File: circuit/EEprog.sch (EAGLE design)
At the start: 27 parts, among them IC1 ATMEGA168-20P, IC2 7400N, IC3 74HCT574N, IC4 74HCT574N, X1 PN61729-S

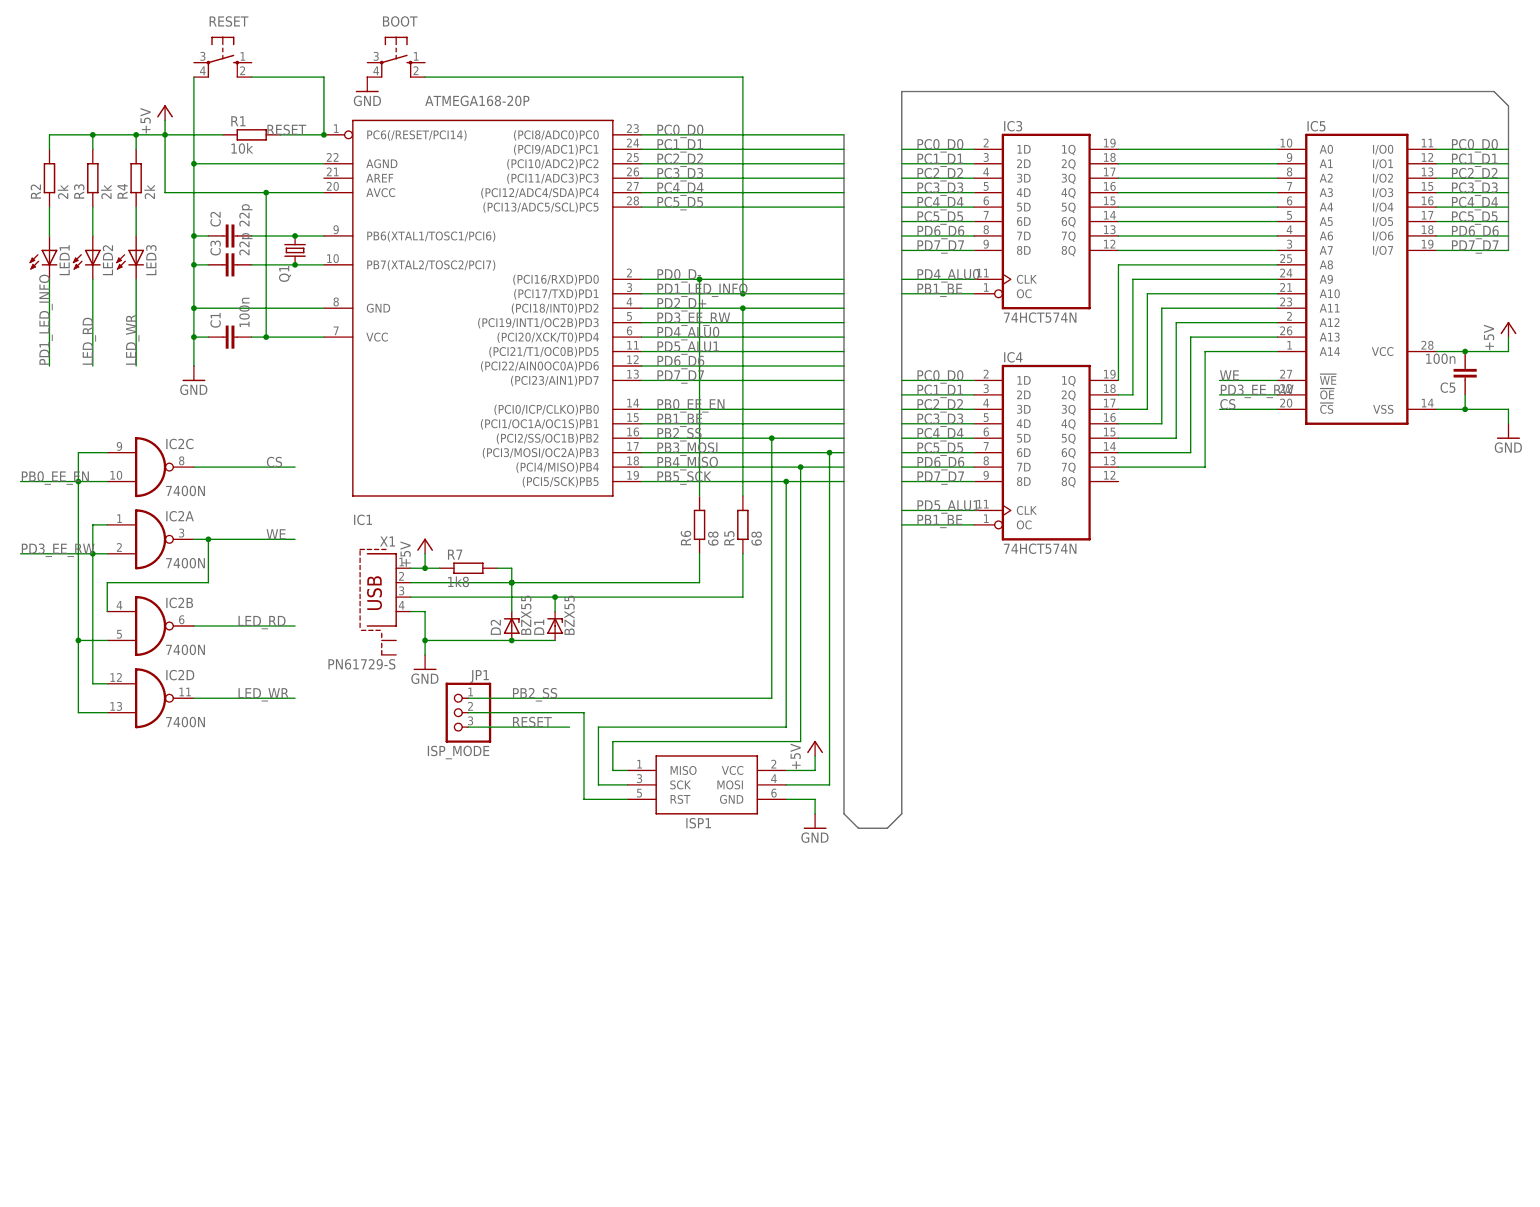
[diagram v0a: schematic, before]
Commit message: updated circuit
durring coldstart of MCU eeprom cell 0x0000 was erased with 0xff value.
pull-down registors on ce & rw control pins fixed issue
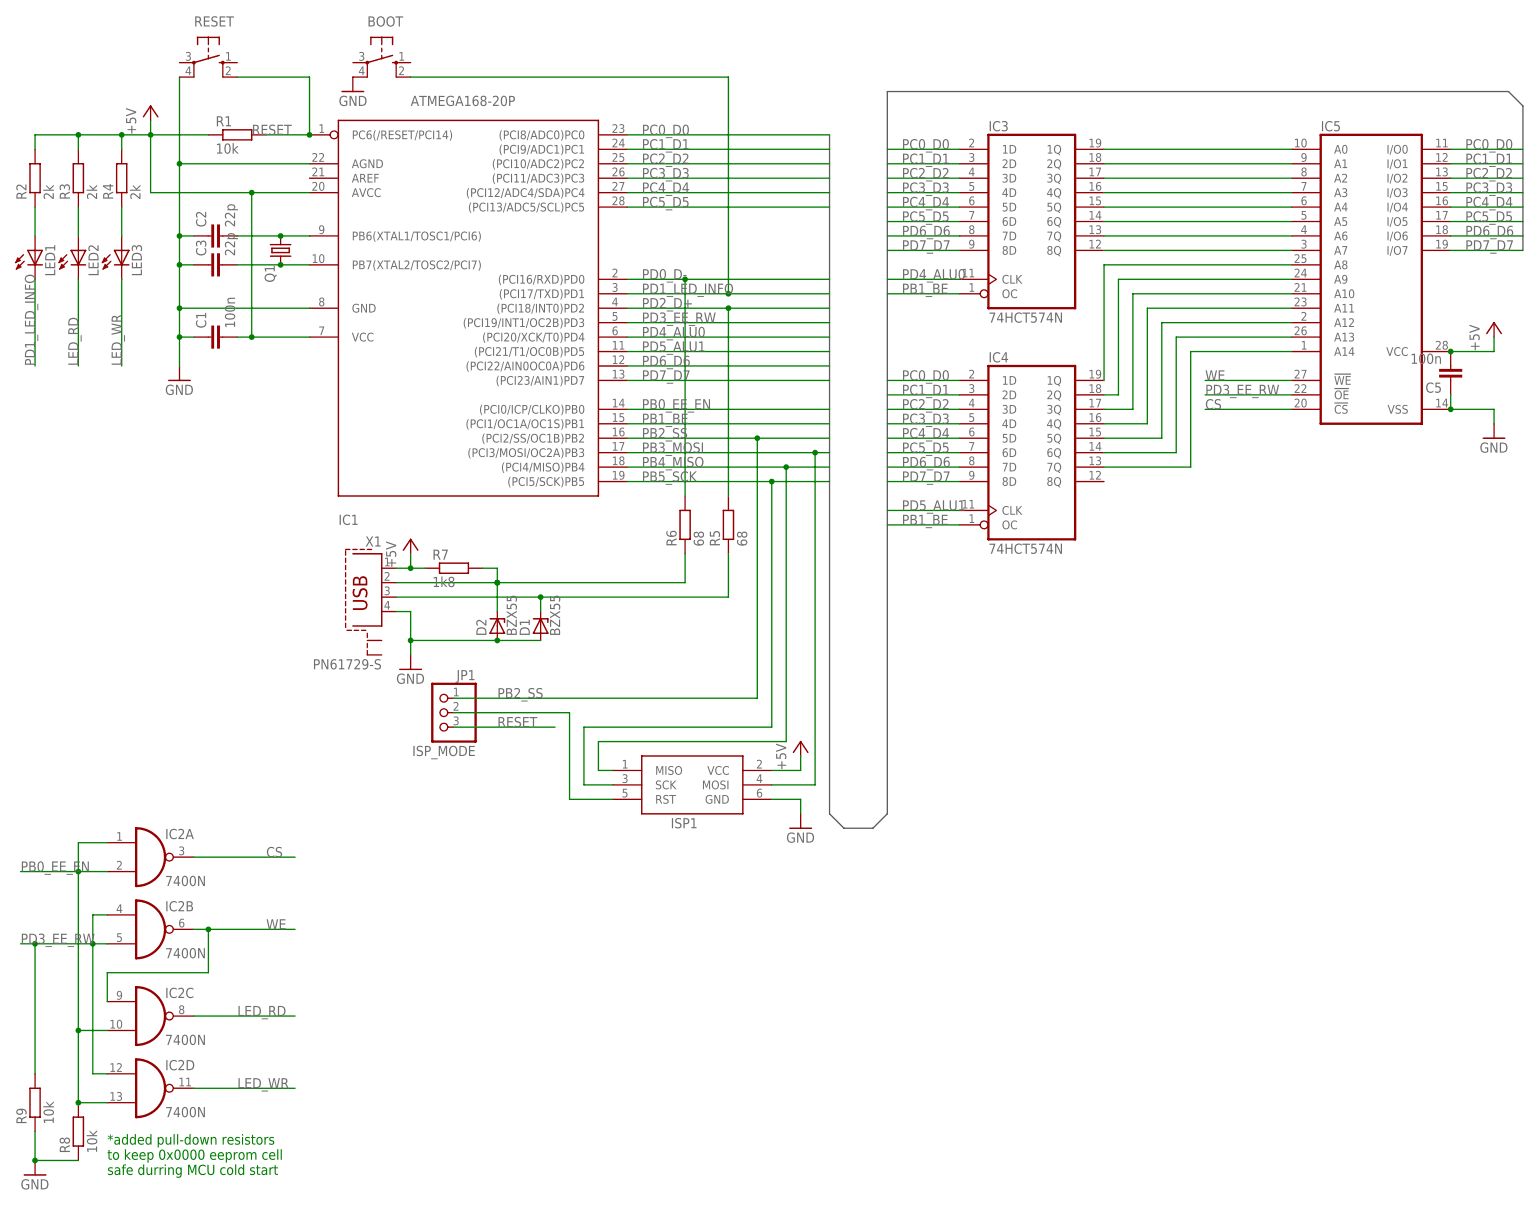
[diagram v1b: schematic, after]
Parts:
- added R8, R9: 10k, resistor:R-EU_0204/7
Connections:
- net CS: now also IC2A.O; no longer IC2C.O
- net GND: now also R8.1, R9.1
- net LED_RD: now also IC2C.O; no longer IC2B.O
- net PB0_EE_EN: now also IC2A.I0, IC2A.I1, R8.2; no longer IC2B.I1, IC2C.I0
- net PD3_EE_RW: now also IC2B.I0, IC2B.I1, R9.2; no longer IC2A.I0, IC2A.I1
- net WE: now also IC2B.O, IC2C.I0; no longer IC2A.O, IC2B.I0
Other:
- note added: "*added pull-down resistors to keep 0x0000 eeprom cell safe durring MCU cold start"
- moved on the sheet: BOOT, C1, C2, C3, C5, D1, D2, IC1, IC2A, IC2B, IC2C, IC2D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
